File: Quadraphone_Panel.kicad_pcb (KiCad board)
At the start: 2 copper layers, 60.8 x 128.5 mm, 30 parts

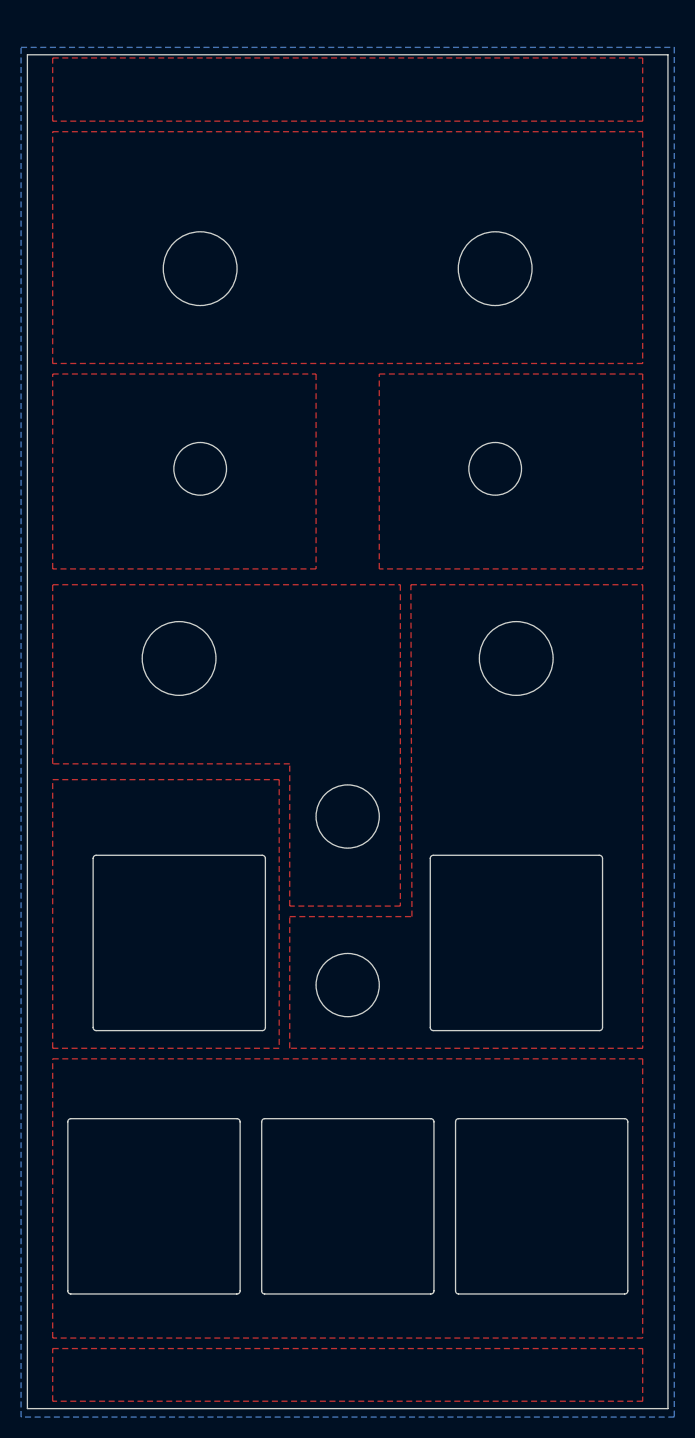
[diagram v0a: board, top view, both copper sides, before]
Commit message: Fixed ground connections on component board
Added JLC PCB plug-in
Schematic clean-up
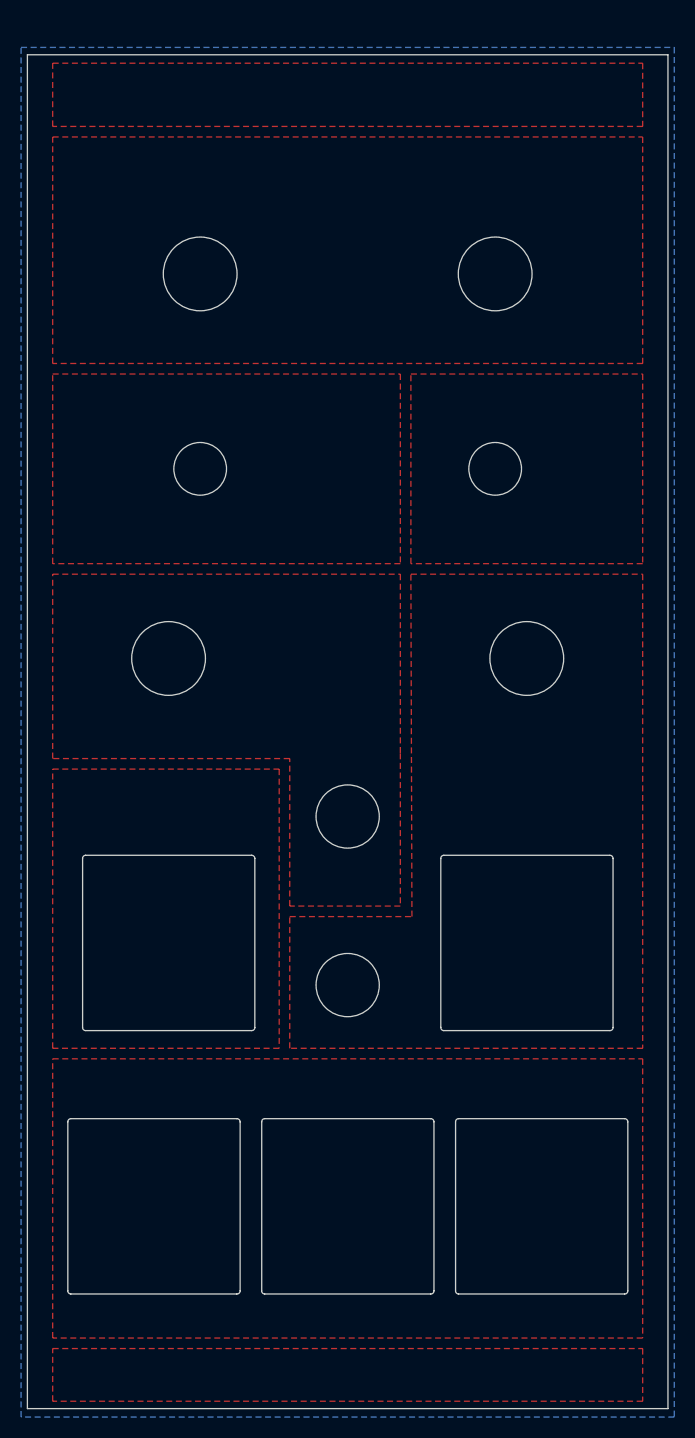
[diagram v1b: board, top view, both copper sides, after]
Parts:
- removed kibuzzard-63D1288B: G***, kibuzzard-63D1288B
- removed kibuzzard-63D139F5: G***, kibuzzard-63D139F5
- removed kibuzzard-63D1404C: G***, kibuzzard-63D1404C
- added kibuzzard-63D25E01: G***, kibuzzard-63D25E01, F.Cu at (90.0, 70.0)
- added kibuzzard-63D25EC7: G***, kibuzzard-63D25EC7, F.Cu at (80.0, 100.1)
- added kibuzzard-63D2A377: G***, kibuzzard-63D2A377, F.Cu at (62.0, 134.5)
- added kibuzzard-63D2A3C5: G***, kibuzzard-63D2A3C5, F.Cu at (80.0, 134.5)
- moved kibuzzard-63D139E5 4.53 mm to (63.0, 108.5)
- moved FM_In 1.00 mm to (63.0, 121.0)
- moved PWM_In 1.00 mm to (97.0, 121.0)
- moved Ref** 1.00 mm to (97.0, 94.0)
- moved Ref** 1.00 mm to (63.0, 94.0)
- moved kibuzzard-63D12809 1.00 mm to (97.0, 106.6)
- moved kibuzzard-63D1286A 1.00 mm to (90.0, 82.0)
- moved G*** 0.50 mm to (80.0, 40.4)
- moved Ref** 0.50 mm to (66.0, 57.5)
- moved Ref** 0.50 mm to (94.0, 57.5)
- moved kibuzzard-63D12295 0.50 mm to (66.0, 47.5)
- moved kibuzzard-63D122C1 0.50 mm to (94.0, 47.5)
- moved kibuzzard-63D127EA 0.50 mm to (80.0, 57.5)
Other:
- board text added: "Quadraphone Panel v1 Mountjoy Modular"
- board text removed: "Quadraphone Panel v1"

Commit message: Prepared all gerbers
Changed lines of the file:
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@@
     (0 "F.Cu" signal)
     (31 "B.Cu" signal)
-    (32 "B.Adhes" user "B.Adhesive")
-    (33 "F.Adhes" user "F.Adhesive")
     (34 "B.Paste" user)
     (35 "F.Paste" user)
@@
     (40 "Dwgs.User" user "User.Drawings")
     (41 "Cmts.User" user "User.Comments")
-    (42 "Eco1.User" user "User.Eco1")
-    (43 "Eco2.User" user "User.Eco2")
     (44 "Edge.Cuts" user)
     (45 "Margin" user)
@@
     (48 "B.Fab" user)
     (49 "F.Fab" user)
-    (50 "User.1" user)
-    (51 "User.2" user)
-    (52 "User.3" user)
-    (53 "User.4" user)
-    (54 "User.5" user)
-    (55 "User.6" user)
-    (56 "User.7" user)
-    (57 "User.8" user)
-    (58 "User.9" user)
   )
   (setup
@@
       (outputformat 1)
       (mirror false)
-      (drillshape 1)
+      (drillshape 0)
       (scaleselection 1)
-      (outputdirectory "")
+      (outputdirectory "Gerbers/Panel/")
     )
   )
@@
     (attr board_only exclude_from_pos_files exclude_from_bom)
     (fp_text reference "kibuzzard-63D25E01" (at 0 -4.869077) (layer "F.SilkS") hide
-      (effects (font (size 0 0)))
+      (effects (font (size 0 0) (thickness 0.15)))
     )
     (fp_text value "G***" (at 0 4.869077) (layer "F.SilkS") hide
-      (effects (font (size 0 0)))
+      (effects (font (size 0 0) (thickness 0.15)))
     )
     (fp_poly (pts
@@
     (fp_line (start -8.16 -8.02) (end -8.16 8.02) (layer "Edge.Cuts") (width 0.12))
     (fp_arc (start 8.19 8.02) (mid 8.100917 8.238111) (end 7.88 8.32) (layer "Edge.Cuts") (width 0.12))
-    (fp_arc (start 7.88 -8.32) (mid 8.096622 -8.233665) (end 8.19 -8.02) (layer "Edge.Cuts") (width 0.12))
+    (fp_arc (start 7.88 -8.32) (mid 8.096588 -8.233658) (end 8.19 -8.02) (layer "Edge.Cuts") (width 0.12))
     (fp_arc (start -7.88 8.32) (mid -8.081749 8.227632) (end -8.16 8.02) (layer "Edge.Cuts") (width 0.12))
     (fp_arc (start -8.16 -8.02) (mid -8.081443 -8.227347) (end -7.88 -8.32) (layer "Edge.Cuts") (width 0.12))
@@
     (fp_arc (start -8.16 -8.02) (mid -8.081443 -8.227347) (end -7.88 -8.32) (layer "Edge.Cuts") (width 0.12))
     (fp_arc (start 8.19 8.02) (mid 8.100917 8.238111) (end 7.88 8.32) (layer "Edge.Cuts") (width 0.12))
-    (fp_arc (start 7.88 -8.32) (mid 8.096622 -8.233665) (end 8.19 -8.02) (layer "Edge.Cuts") (width 0.12))
+    (fp_arc (start 7.88 -8.32) (mid 8.096588 -8.233658) (end 8.19 -8.02) (layer "Edge.Cuts") (width 0.12))
     (fp_line (start -8.31 -8.5) (end -8.31 8.5) (layer "F.CrtYd") (width 0.05))
     (fp_line (start 8.39 -8.5) (end 8.39 8.5) (layer "F.CrtYd") (width 0.05))
@@
     (attr board_only exclude_from_pos_files exclude_from_bom)
     (fp_text reference "kibuzzard-63D2A377" (at 0 -4.760221) (layer "F.SilkS") hide
-      (effects (font (size 0 0)))
+      (effects (font (size 0 0) (thickness 0.15)))
     )
     (fp_text value "G***" (at 0 4.760221) (layer "F.SilkS") hide
-      (effects (font (size 0 0)))
+      (effects (font (size 0 0) (thickness 0.15)))
     )
     (fp_poly (pts
@@
     (attr board_only exclude_from_pos_files exclude_from_bom)
     (fp_text reference "kibuzzard-63D2A3C5" (at 0 -4.68697) (layer "F.SilkS") hide
-      (effects (font (size 0 0)))
+      (effects (font (size 0 0) (thickness 0.15)))
     )
     (fp_text value "G***" (at 0 4.68697) (layer "F.SilkS") hide
-      (effects (font (size 0 0)))
+      (effects (font (size 0 0) (thickness 0.15)))
     )
     (fp_poly (pts
@@
     (attr board_only exclude_from_pos_files exclude_from_bom)
     (fp_text reference "kibuzzard-63D25EC7" (at 0 -4.728828 90) (layer "F.SilkS") hide
-      (effects (font (size 0 0)))
+      (effects (font (size 0 0) (thickness 0.15)))
     )
     (fp_text value "G***" (at 0 4.728828 90) (layer "F.SilkS") hide
-      (effects (font (size 0 0)))
+      (effects (font (size 0 0) (thickness 0.15)))
     )
     (fp_poly (pts
@@
     (fp_arc (start -8.16 -8.02) (mid -8.081443 -8.227347) (end -7.88 -8.32) (layer "Edge.Cuts") (width 0.12))
     (fp_arc (start 8.19 8.02) (mid 8.100917 8.238111) (end 7.88 8.32) (layer "Edge.Cuts") (width 0.12))
-    (fp_arc (start 7.88 -8.32) (mid 8.096622 -8.233665) (end 8.19 -8.02) (layer "Edge.Cuts") (width 0.12))
+    (fp_arc (start 7.88 -8.32) (mid 8.096588 -8.233658) (end 8.19 -8.02) (layer "Edge.Cuts") (width 0.12))
     (fp_line (start 8.39 -8.5) (end 8.39 8.5) (layer "F.CrtYd") (width 0.05))
     (fp_line (start -8.31 -8.5) (end -8.31 8.5) (layer "F.CrtYd") (width 0.05))
@@
     (fp_line (start 7.88 -8.32) (end -7.88 -8.32) (layer "Edge.Cuts") (width 0.12))
     (fp_arc (start -7.88 8.32) (mid -8.081749 8.227632) (end -8.16 8.02) (layer "Edge.Cuts") (width 0.12))
-    (fp_arc (start 7.88 -8.32) (mid 8.096622 -8.233665) (end 8.19 -8.02) (layer "Edge.Cuts") (width 0.12))
+    (fp_arc (start 7.88 -8.32) (mid 8.096588 -8.233658) (end 8.19 -8.02) (layer "Edge.Cuts") (width 0.12))
     (fp_arc (start -8.16 -8.02) (mid -8.081443 -8.227347) (end -7.88 -8.32) (layer "Edge.Cuts") (width 0.12))
     (fp_arc (start 8.19 8.02) (mid 8.100917 8.238111) (end 7.88 8.32) (layer "Edge.Cuts") (width 0.12))
@@
     (fp_line (start -8.16 -8.02) (end -8.16 8.02) (layer "Edge.Cuts") (width 0.12))
     (fp_arc (start -7.88 8.32) (mid -8.081749 8.227632) (end -8.16 8.02) (layer "Edge.Cuts") (width 0.12))
-    (fp_arc (start 7.88 -8.32) (mid 8.096622 -8.233665) (end 8.19 -8.02) (layer "Edge.Cuts") (width 0.12))
+    (fp_arc (start 7.88 -8.32) (mid 8.096588 -8.233658) (end 8.19 -8.02) (layer "Edge.Cuts") (width 0.12))
     (fp_arc (start 8.19 8.02) (mid 8.100917 8.238111) (end 7.88 8.32) (layer "Edge.Cuts") (width 0.12))
     (fp_arc (start -8.16 -8.02) (mid -8.081443 -8.227347) (end -7.88 -8.32) (layer "Edge.Cuts") (width 0.12))

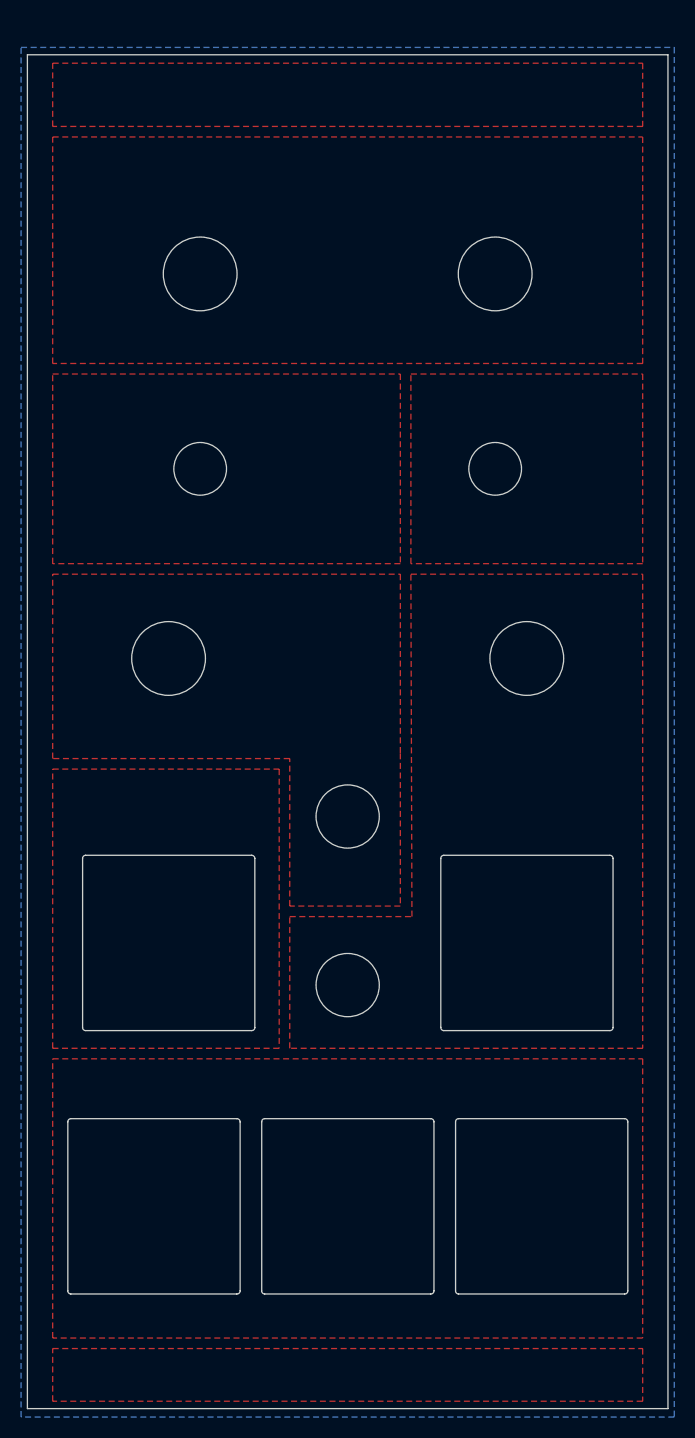
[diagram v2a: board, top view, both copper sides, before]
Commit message: Fixed issue with hole for voice switch size
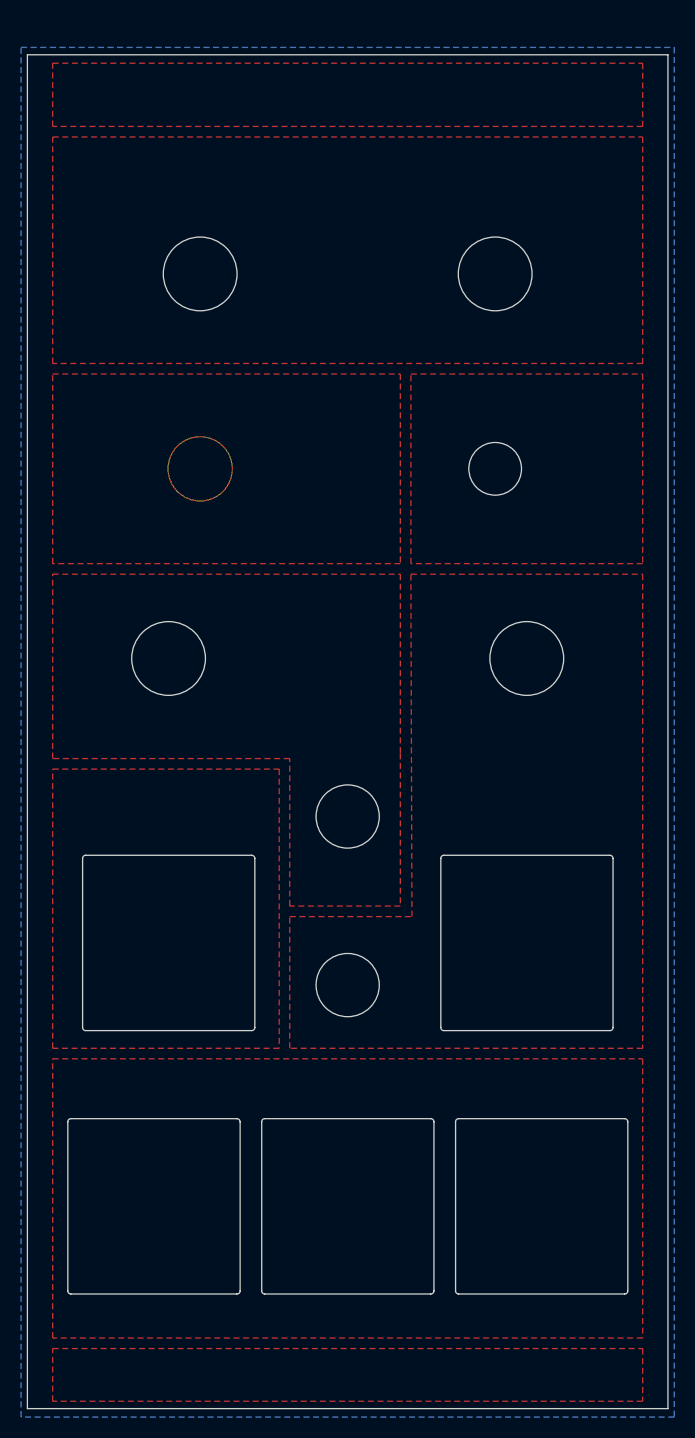
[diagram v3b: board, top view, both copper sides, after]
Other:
- board text added: "Quadraphone Panel v1.1 Mountjoy Modular"
- board text removed: "Quadraphone Panel v1 Mountjoy Modular"
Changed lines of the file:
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@@
     (fp_line (start -8.16 -8.02) (end -8.16 8.02) (layer "Edge.Cuts") (width 0.12))
     (fp_arc (start 8.19 8.02) (mid 8.100917 8.238111) (end 7.88 8.32) (layer "Edge.Cuts") (width 0.12))
-    (fp_arc (start 7.88 -8.32) (mid 8.096588 -8.233658) (end 8.19 -8.02) (layer "Edge.Cuts") (width 0.12))
+    (fp_arc (start 7.88 -8.32) (mid 8.096622 -8.233665) (end 8.19 -8.02) (layer "Edge.Cuts") (width 0.12))
     (fp_arc (start -7.88 8.32) (mid -8.081749 8.227632) (end -8.16 8.02) (layer "Edge.Cuts") (width 0.12))
     (fp_arc (start -8.16 -8.02) (mid -8.081443 -8.227347) (end -7.88 -8.32) (layer "Edge.Cuts") (width 0.12))
@@
     (fp_arc (start -8.16 -8.02) (mid -8.081443 -8.227347) (end -7.88 -8.32) (layer "Edge.Cuts") (width 0.12))
     (fp_arc (start 8.19 8.02) (mid 8.100917 8.238111) (end 7.88 8.32) (layer "Edge.Cuts") (width 0.12))
-    (fp_arc (start 7.88 -8.32) (mid 8.096588 -8.233658) (end 8.19 -8.02) (layer "Edge.Cuts") (width 0.12))
+    (fp_arc (start 7.88 -8.32) (mid 8.096622 -8.233665) (end 8.19 -8.02) (layer "Edge.Cuts") (width 0.12))
     (fp_line (start -8.31 -8.5) (end -8.31 8.5) (layer "F.CrtYd") (width 0.05))
     (fp_line (start 8.39 -8.5) (end 8.39 8.5) (layer "F.CrtYd") (width 0.05))
@@
     (fp_circle (center 0 0) (end 2.5 0) (layer "Cmts.User") (width 0.15) (fill none))
     (fp_circle (center 0 0) (end 4 0) (layer "F.CrtYd") (width 0.05) (fill none))
-    (pad "" np_thru_hole circle (at 0 0) (size 5 5) (drill 5) (layers *.Cu *.Mask))
+    (pad "" np_thru_hole circle (at 0 0) (size 6.2 6.2) (drill 6) (layers F&B.Cu *.Mask))
     (model "${CUSTOM_3D}/Eledis 1A11-NF1STSE SPDT Toggle Switch.stp"
       (offset (xyz 0 3.8 -10.5))
@@
     (fp_arc (start -8.16 -8.02) (mid -8.081443 -8.227347) (end -7.88 -8.32) (layer "Edge.Cuts") (width 0.12))
     (fp_arc (start 8.19 8.02) (mid 8.100917 8.238111) (end 7.88 8.32) (layer "Edge.Cuts") (width 0.12))
-    (fp_arc (start 7.88 -8.32) (mid 8.096588 -8.233658) (end 8.19 -8.02) (layer "Edge.Cuts") (width 0.12))
+    (fp_arc (start 7.88 -8.32) (mid 8.096622 -8.233665) (end 8.19 -8.02) (layer "Edge.Cuts") (width 0.12))
     (fp_line (start 8.39 -8.5) (end 8.39 8.5) (layer "F.CrtYd") (width 0.05))
     (fp_line (start -8.31 -8.5) (end -8.31 8.5) (layer "F.CrtYd") (width 0.05))
@@
     (fp_line (start 7.88 -8.32) (end -7.88 -8.32) (layer "Edge.Cuts") (width 0.12))
     (fp_arc (start -7.88 8.32) (mid -8.081749 8.227632) (end -8.16 8.02) (layer "Edge.Cuts") (width 0.12))
-    (fp_arc (start 7.88 -8.32) (mid 8.096588 -8.233658) (end 8.19 -8.02) (layer "Edge.Cuts") (width 0.12))
+    (fp_arc (start 7.88 -8.32) (mid 8.096622 -8.233665) (end 8.19 -8.02) (layer "Edge.Cuts") (width 0.12))
     (fp_arc (start -8.16 -8.02) (mid -8.081443 -8.227347) (end -7.88 -8.32) (layer "Edge.Cuts") (width 0.12))
     (fp_arc (start 8.19 8.02) (mid 8.100917 8.238111) (end 7.88 8.32) (layer "Edge.Cuts") (width 0.12))
@@
     (fp_line (start -8.16 -8.02) (end -8.16 8.02) (layer "Edge.Cuts") (width 0.12))
     (fp_arc (start -7.88 8.32) (mid -8.081749 8.227632) (end -8.16 8.02) (layer "Edge.Cuts") (width 0.12))
-    (fp_arc (start 7.88 -8.32) (mid 8.096588 -8.233658) (end 8.19 -8.02) (layer "Edge.Cuts") (width 0.12))
+    (fp_arc (start 7.88 -8.32) (mid 8.096622 -8.233665) (end 8.19 -8.02) (layer "Edge.Cuts") (width 0.12))
     (fp_arc (start 8.19 8.02) (mid 8.100917 8.238111) (end 7.88 8.32) (layer "Edge.Cuts") (width 0.12))
     (fp_arc (start -8.16 -8.02) (mid -8.081443 -8.227347) (end -7.88 -8.32) (layer "Edge.Cuts") (width 0.12))
@@
   (gr_line (start 110.4 36.7) (end 110.4 165.2) (layer "Edge.Cuts") (width 0.1))
   (gr_line (start 49.6 36.7) (end 110.4 36.7) (layer "Edge.Cuts") (width 0.1))
-  (gr_text "Quadraphone Panel v1\nMountjoy Modular" (at 80 42.5) (layer "B.SilkS")
+  (gr_text "Quadraphone Panel v1.1\nMountjoy Modular" (at 80 42.5) (layer "B.SilkS")
     (effects (font (size 1.5 1.5) (thickness 0.3)) (justify mirror))
   )

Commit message: Clean up control board
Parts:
- moved FM_In 2.50 mm to (63.0, 118.5)
- moved G*** 2.50 mm to (80.0, 37.9)
- moved Output 2.50 mm to (80.0, 143.5)
- moved PWM_In 2.50 mm to (97.0, 118.5)
- moved Ref** 2.50 mm to (94.0, 73.5)
- moved Ref** 2.50 mm to (57.1, 159.7)
- moved Ref** 2.50 mm to (80.0, 106.5)
- moved Ref** 2.50 mm to (57.1, 37.2)
- moved Ref** 2.50 mm to (66.0, 55.0)
- moved Ref** 2.50 mm to (102.9, 37.2)
- moved Ref** 2.50 mm to (94.0, 55.0)
- moved Ref** 2.50 mm to (97.0, 91.5)
- moved Ref** 2.50 mm to (66.0, 73.5)
- moved Ref** 2.50 mm to (102.9, 159.7)
- moved Ref** 2.50 mm to (80.0, 122.5)
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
